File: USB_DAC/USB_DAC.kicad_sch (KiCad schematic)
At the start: 65 parts, among them J1 USB_B, J2 DAC_OUT_L, J3 DAC_OUT_R, Q1 BC847, U1 MIC5205YM5, U2 USBLC6-2SC6, U3 OPA2353UA, U4 PCM2900, Y1 12MHz 18pF

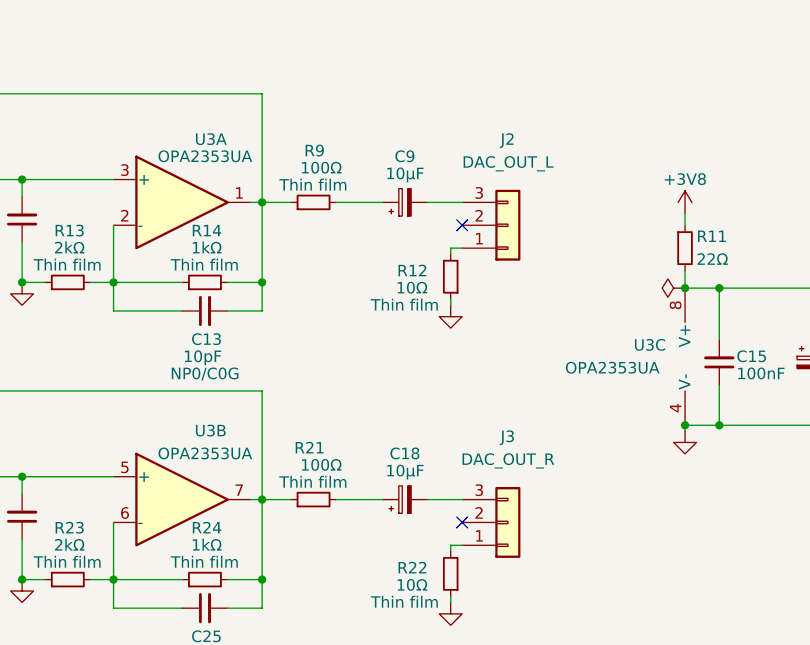
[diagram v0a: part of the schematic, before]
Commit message: Changed capacitor values
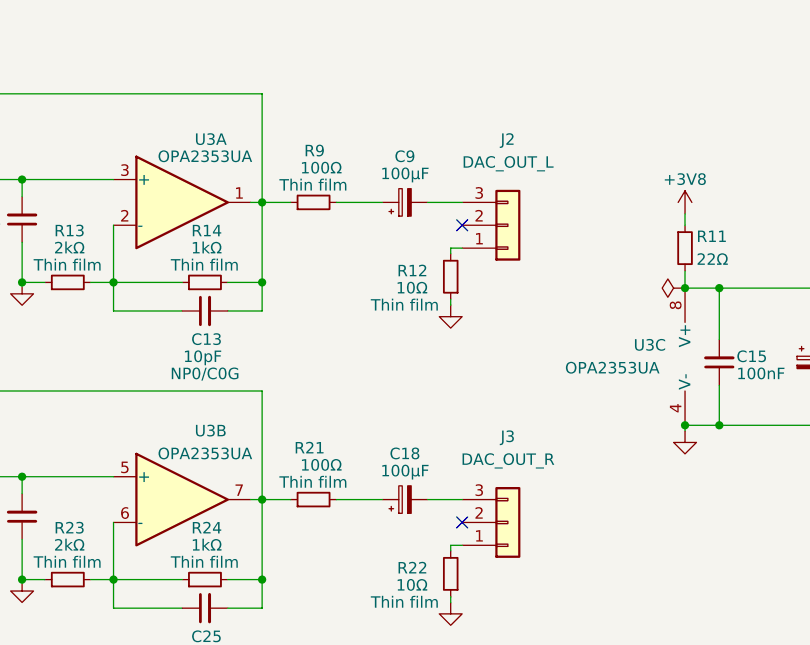
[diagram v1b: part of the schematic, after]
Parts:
- C18, C9: value 10µF -> 100µF
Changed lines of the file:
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@@
       (effects (font (size 1.27 1.27)))
     )
-    (property "Value" "10µF" (at 220.98 137.795 90)
+    (property "Value" "100µF" (at 220.98 137.795 90)
       (effects (font (size 1.27 1.27)))
     )
@@
       (effects (font (size 1.27 1.27)))
     )
-    (property "Value" "10µF" (at 220.98 104.775 90)
-      (effects (font (size 1.27 1.27)))
-    )
+    (property "Value" "100µF" (at 220.98 104.775 90)
+      (effects (font (size 1.27 1.27)))
+    )

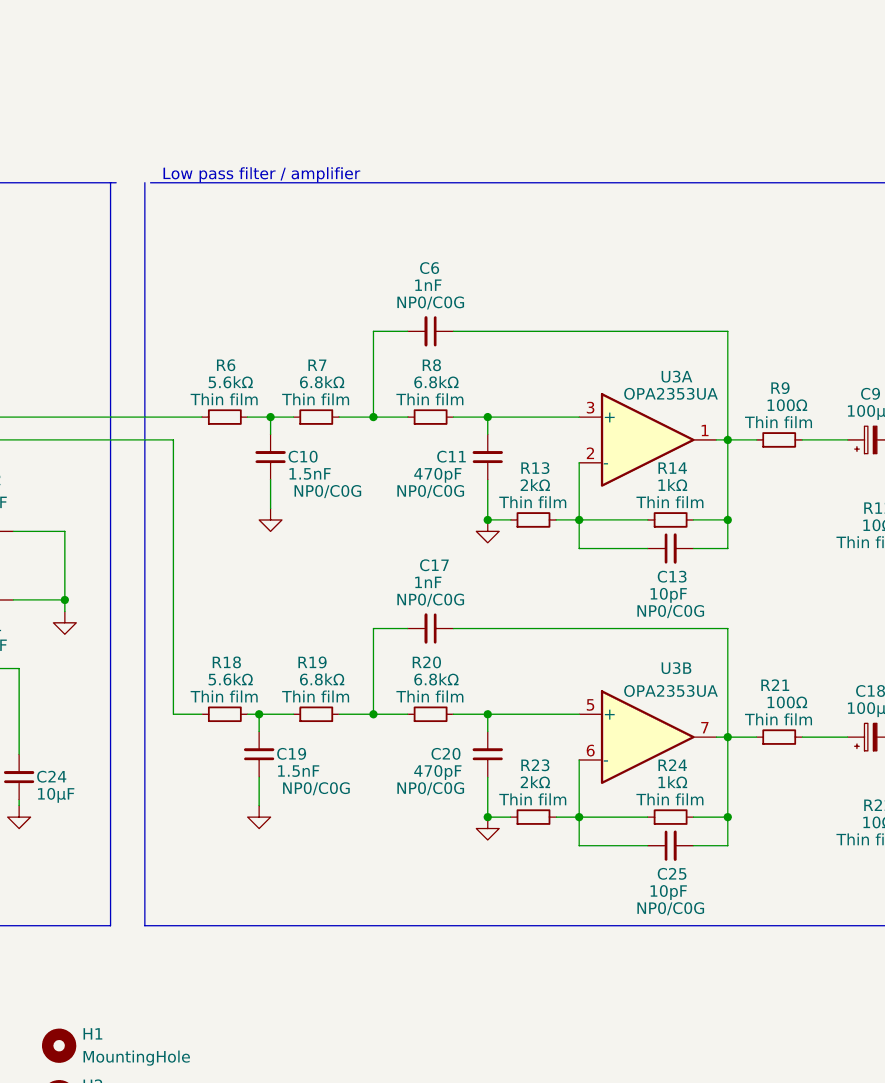
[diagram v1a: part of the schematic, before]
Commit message: Feedback resistors changed for 0dB gain
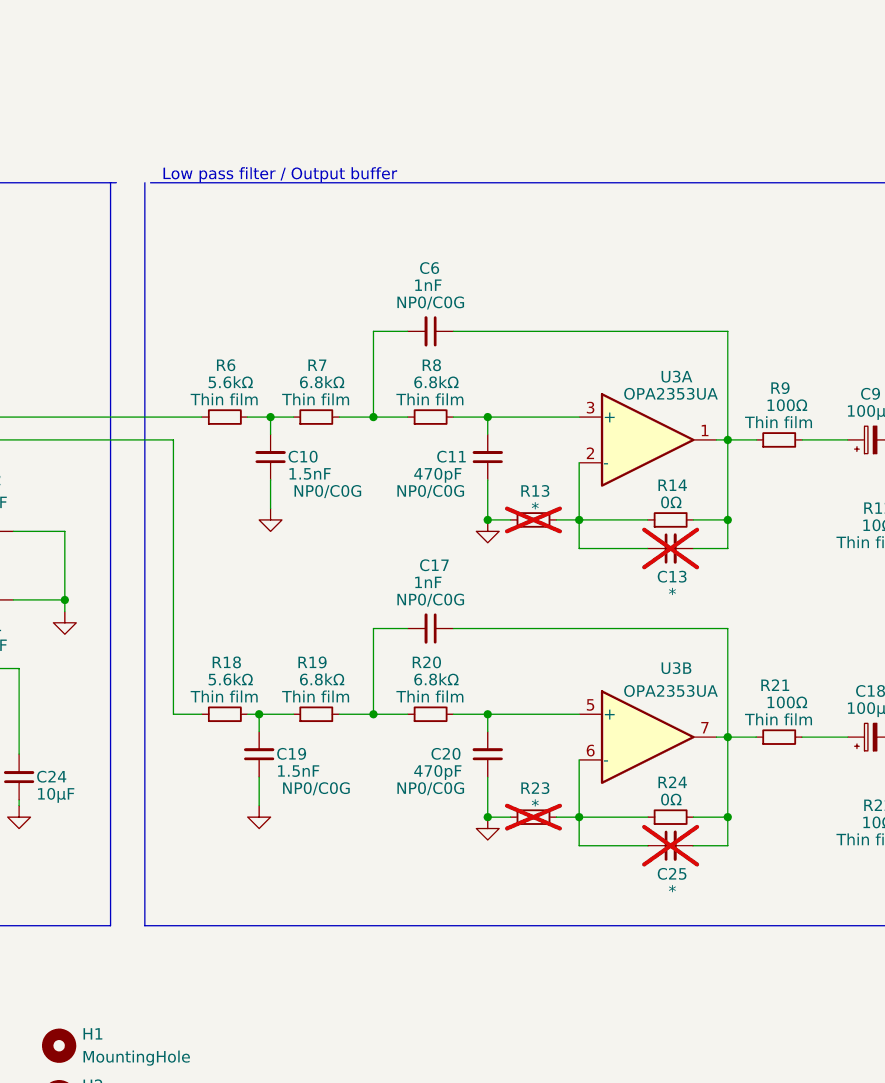
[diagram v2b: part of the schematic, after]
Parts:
- C13, C25: value 10pF -> *; now not fitted
- R13, R23: value 2kΩ -> *; now not fitted
- R14, R24: value 1kΩ -> 0Ω
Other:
- note added: "Low pass filter / Output buffer"
- note removed: "Low pass filter / amplifier"
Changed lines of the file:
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@@
     (effects (font (size 1.27 1.27)) (justify left bottom))
   )
-  (text "Low pass filter / amplifier" (at 142.24 79.375 0)
+  (text "Low pass filter / Output buffer" (at 142.24 79.375 0)
     (effects (font (size 1.27 1.27)) (justify left bottom))
   )
@@
   )
   (symbol (lib_id "Device:C_Small") (at 198.755 120.015 90) (mirror x) (unit 1)
-    (in_bom yes) (on_board yes) (dnp no)
+    (in_bom yes) (on_board yes) (dnp yes)
     (property "Reference" "C13" (at 200.66 123.19 90)
       (effects (font (size 1.27 1.27)) (justify left))
     )
-    (property "Value" "10pF" (at 200.66 125.095 90)
+    (property "Value" "*" (at 199.39 125.095 90)
       (effects (font (size 1.27 1.27)) (justify left))
     )
@@
     )
     (property "Comments" "NP0/C0G" (at 198.755 127 90)
-      (effects (font (size 1.27 1.27)))
+      (effects (font (size 1.27 1.27)) hide)
     )
     (pin "1")
@@
   )
   (symbol (lib_id "Device:C_Small") (at 198.755 153.035 90) (mirror x) (unit 1)
-    (in_bom yes) (on_board yes) (dnp no)
+    (in_bom yes) (on_board yes) (dnp yes)
     (property "Reference" "C25" (at 200.66 156.21 90)
       (effects (font (size 1.27 1.27)) (justify left))
     )
-    (property "Value" "10pF" (at 200.66 158.115 90)
+    (property "Value" "*" (at 199.39 158.115 90)
       (effects (font (size 1.27 1.27)) (justify left))
     )
@@
     )
     (property "Comments" "NP0/C0G" (at 198.755 160.02 90)
-      (effects (font (size 1.27 1.27)))
+      (effects (font (size 1.27 1.27)) hide)
     )
     (pin "1")
@@
   (symbol (lib_id "Device:R_Small") (at 198.755 116.84 90) (unit 1)
     (in_bom yes) (on_board yes) (dnp no)
-    (property "Reference" "R14" (at 200.66 111.125 90)
-      (effects (font (size 1.27 1.27)) (justify left))
-    )
-    (property "Value" "1kΩ" (at 200.66 113.03 90)
+    (property "Reference" "R14" (at 200.66 113.03 90)
+      (effects (font (size 1.27 1.27)) (justify left))
+    )
+    (property "Value" "0Ω" (at 200.025 114.935 90)
       (effects (font (size 1.27 1.27)) (justify left))
     )
@@
     )
     (property "Comments" "Thin film" (at 198.755 114.935 90)
-      (effects (font (size 1.27 1.27)))
+      (effects (font (size 1.27 1.27)) hide)
     )
     (pin "1")
@@
   (symbol (lib_id "Device:R_Small") (at 198.755 149.86 90) (unit 1)
     (in_bom yes) (on_board yes) (dnp no)
-    (property "Reference" "R24" (at 200.66 144.145 90)
-      (effects (font (size 1.27 1.27)) (justify left))
-    )
-    (property "Value" "1kΩ" (at 200.66 146.05 90)
+    (property "Reference" "R24" (at 200.66 146.05 90)
+      (effects (font (size 1.27 1.27)) (justify left))
+    )
+    (property "Value" "0Ω" (at 200.025 147.955 90)
       (effects (font (size 1.27 1.27)) (justify left))
     )
@@
     )
     (property "Comments" "Thin film" (at 198.755 147.955 90)
-      (effects (font (size 1.27 1.27)))
+      (effects (font (size 1.27 1.27)) hide)
     )
     (pin "1")
@@
   )
   (symbol (lib_id "Device:R_Small") (at 183.515 149.86 90) (unit 1)
-    (in_bom yes) (on_board yes) (dnp no)
-    (property "Reference" "R23" (at 185.42 144.145 90)
-      (effects (font (size 1.27 1.27)) (justify left))
-    )
-    (property "Value" "2kΩ" (at 185.42 146.05 90)
+    (in_bom yes) (on_board yes) (dnp yes)
+    (property "Reference" "R23" (at 185.42 146.685 90)
+      (effects (font (size 1.27 1.27)) (justify left))
+    )
+    (property "Value" "*" (at 184.15 148.59 90)
       (effects (font (size 1.27 1.27)) (justify left))
     )
@@
     )
     (property "Comments" "Thin film" (at 183.515 147.955 90)
-      (effects (font (size 1.27 1.27)))
+      (effects (font (size 1.27 1.27)) hide)
     )
     (pin "1")
@@
   )
   (symbol (lib_id "Device:R_Small") (at 183.515 116.84 90) (unit 1)
-    (in_bom yes) (on_board yes) (dnp no)
-    (property "Reference" "R13" (at 185.42 111.125 90)
-      (effects (font (size 1.27 1.27)) (justify left))
-    )
-    (property "Value" "2kΩ" (at 185.42 113.03 90)
+    (in_bom yes) (on_board yes) (dnp yes)
+    (property "Reference" "R13" (at 185.42 113.665 90)
+      (effects (font (size 1.27 1.27)) (justify left))
+    )
+    (property "Value" "*" (at 184.15 115.57 90)
       (effects (font (size 1.27 1.27)) (justify left))
     )
@@
     )
     (property "Comments" "Thin film" (at 183.515 114.935 90)
-      (effects (font (size 1.27 1.27)))
-    )
-    (pin "1")
+      (effects (font (size 1.27 1.27)) hide)
+    )
+    (pin "1")

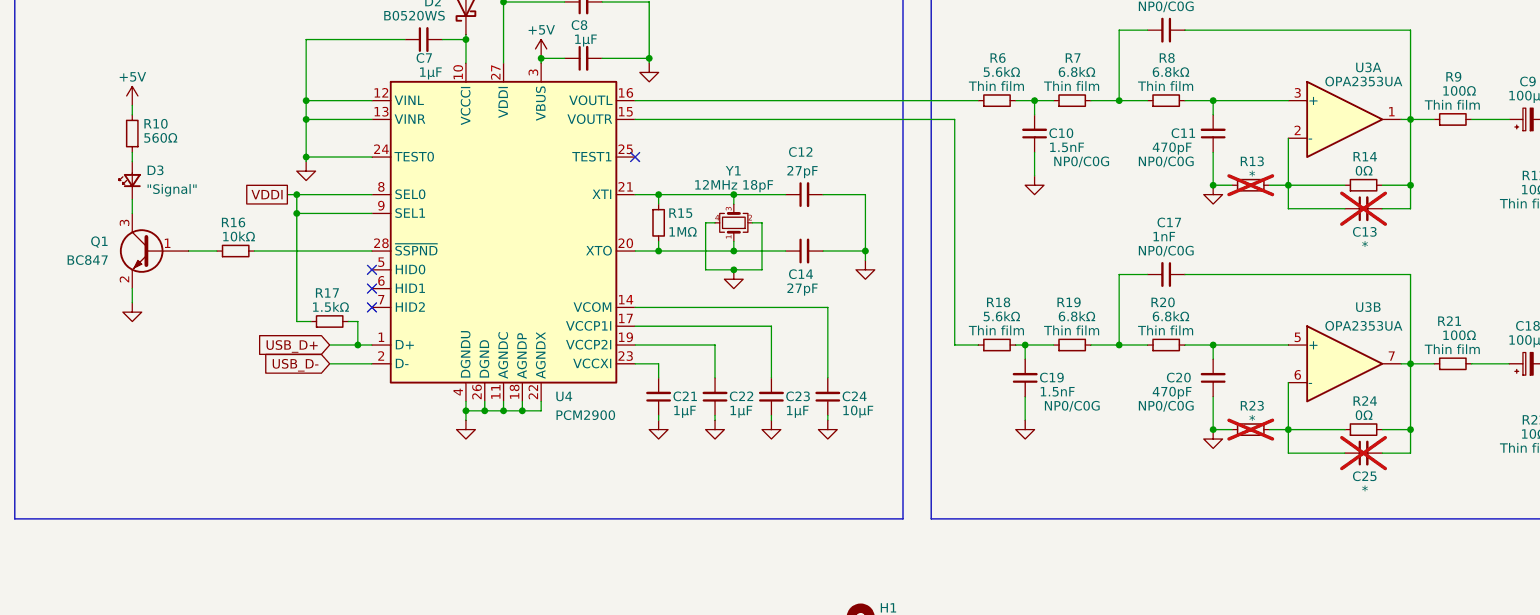
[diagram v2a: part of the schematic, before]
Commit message: Changed component values
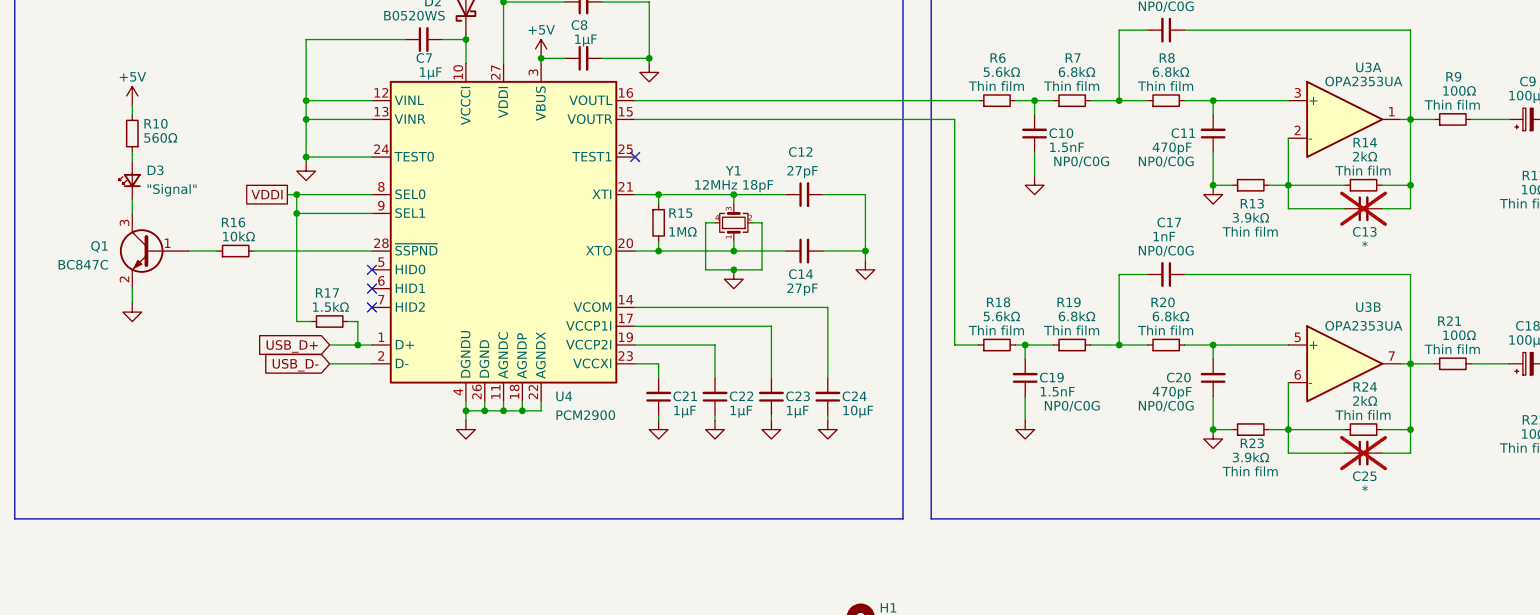
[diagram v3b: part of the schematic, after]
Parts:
- Q1: value BC847 -> BC847C
- R13, R23: value * -> 3.9kΩ; now fitted
- R14, R24: value 0Ω -> 2kΩ
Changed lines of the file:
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@@
   (symbol (lib_id "Device:R_Small") (at 198.755 116.84 90) (unit 1)
     (in_bom yes) (on_board yes) (dnp no)
-    (property "Reference" "R14" (at 200.66 113.03 90)
-      (effects (font (size 1.27 1.27)) (justify left))
-    )
-    (property "Value" "0Ω" (at 200.025 114.935 90)
+    (property "Reference" "R14" (at 200.66 111.125 90)
+      (effects (font (size 1.27 1.27)) (justify left))
+    )
+    (property "Value" "2kΩ" (at 200.66 113.03 90)
       (effects (font (size 1.27 1.27)) (justify left))
     )
@@
     )
     (property "Comments" "Thin film" (at 198.755 114.935 90)
-      (effects (font (size 1.27 1.27)) hide)
+      (effects (font (size 1.27 1.27)))
     )
     (pin "1")
@@
   (symbol (lib_id "Transistor_BJT:BC847") (at 34.925 125.73 0) (mirror y) (unit 1)
     (in_bom yes) (on_board yes) (dnp no) (fields_autoplaced)
-    (property "Reference" "Q1" (at 29.21 124.4599 0)
-      (effects (font (size 1.27 1.27)) (justify left))
-    )
-    (property "Value" "BC847" (at 29.21 126.9999 0)
+    (property "Reference" "Q1" (at 29.21 125.095 0)
+      (effects (font (size 1.27 1.27)) (justify left))
+    )
+    (property "Value" "BC847C" (at 29.21 127.635 0)
       (effects (font (size 1.27 1.27)) (justify left))
     )
@@
   (symbol (lib_id "Device:R_Small") (at 198.755 149.86 90) (unit 1)
     (in_bom yes) (on_board yes) (dnp no)
-    (property "Reference" "R24" (at 200.66 146.05 90)
-      (effects (font (size 1.27 1.27)) (justify left))
-    )
-    (property "Value" "0Ω" (at 200.025 147.955 90)
+    (property "Reference" "R24" (at 200.66 144.145 90)
+      (effects (font (size 1.27 1.27)) (justify left))
+    )
+    (property "Value" "2kΩ" (at 200.66 146.05 90)
       (effects (font (size 1.27 1.27)) (justify left))
     )
@@
     )
     (property "Comments" "Thin film" (at 198.755 147.955 90)
-      (effects (font (size 1.27 1.27)) hide)
+      (effects (font (size 1.27 1.27)))
     )
     (pin "1")
@@
   )
   (symbol (lib_id "Device:R_Small") (at 183.515 149.86 90) (unit 1)
-    (in_bom yes) (on_board yes) (dnp yes)
-    (property "Reference" "R23" (at 185.42 146.685 90)
-      (effects (font (size 1.27 1.27)) (justify left))
-    )
-    (property "Value" "*" (at 184.15 148.59 90)
+    (in_bom yes) (on_board yes) (dnp no)
+    (property "Reference" "R23" (at 185.42 151.765 90)
+      (effects (font (size 1.27 1.27)) (justify left))
+    )
+    (property "Value" "3.9kΩ" (at 186.055 153.67 90)
       (effects (font (size 1.27 1.27)) (justify left))
     )
@@
       (effects (font (size 1.27 1.27)) hide)
     )
-    (property "Comments" "Thin film" (at 183.515 147.955 90)
-      (effects (font (size 1.27 1.27)) hide)
+    (property "Comments" "Thin film" (at 183.515 155.575 90)
+      (effects (font (size 1.27 1.27)))
     )
     (pin "1")
@@
   )
   (symbol (lib_id "Device:R_Small") (at 183.515 116.84 90) (unit 1)
-    (in_bom yes) (on_board yes) (dnp yes)
-    (property "Reference" "R13" (at 185.42 113.665 90)
-      (effects (font (size 1.27 1.27)) (justify left))
-    )
-    (property "Value" "*" (at 184.15 115.57 90)
+    (in_bom yes) (on_board yes) (dnp no)
+    (property "Reference" "R13" (at 185.42 119.38 90)
+      (effects (font (size 1.27 1.27)) (justify left))
+    )
+    (property "Value" "3.9kΩ" (at 186.055 121.285 90)
       (effects (font (size 1.27 1.27)) (justify left))
     )
@@
       (effects (font (size 1.27 1.27)) hide)
     )
-    (property "Comments" "Thin film" (at 183.515 114.935 90)
-      (effects (font (size 1.27 1.27)) hide)
-    )
-    (pin "1")
+    (property "Comments" "Thin film" (at 183.515 123.19 90)
+      (effects (font (size 1.27 1.27)))
+    )
+    (pin "1")
